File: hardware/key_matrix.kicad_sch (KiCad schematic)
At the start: 2 parts, among them SW3 Key

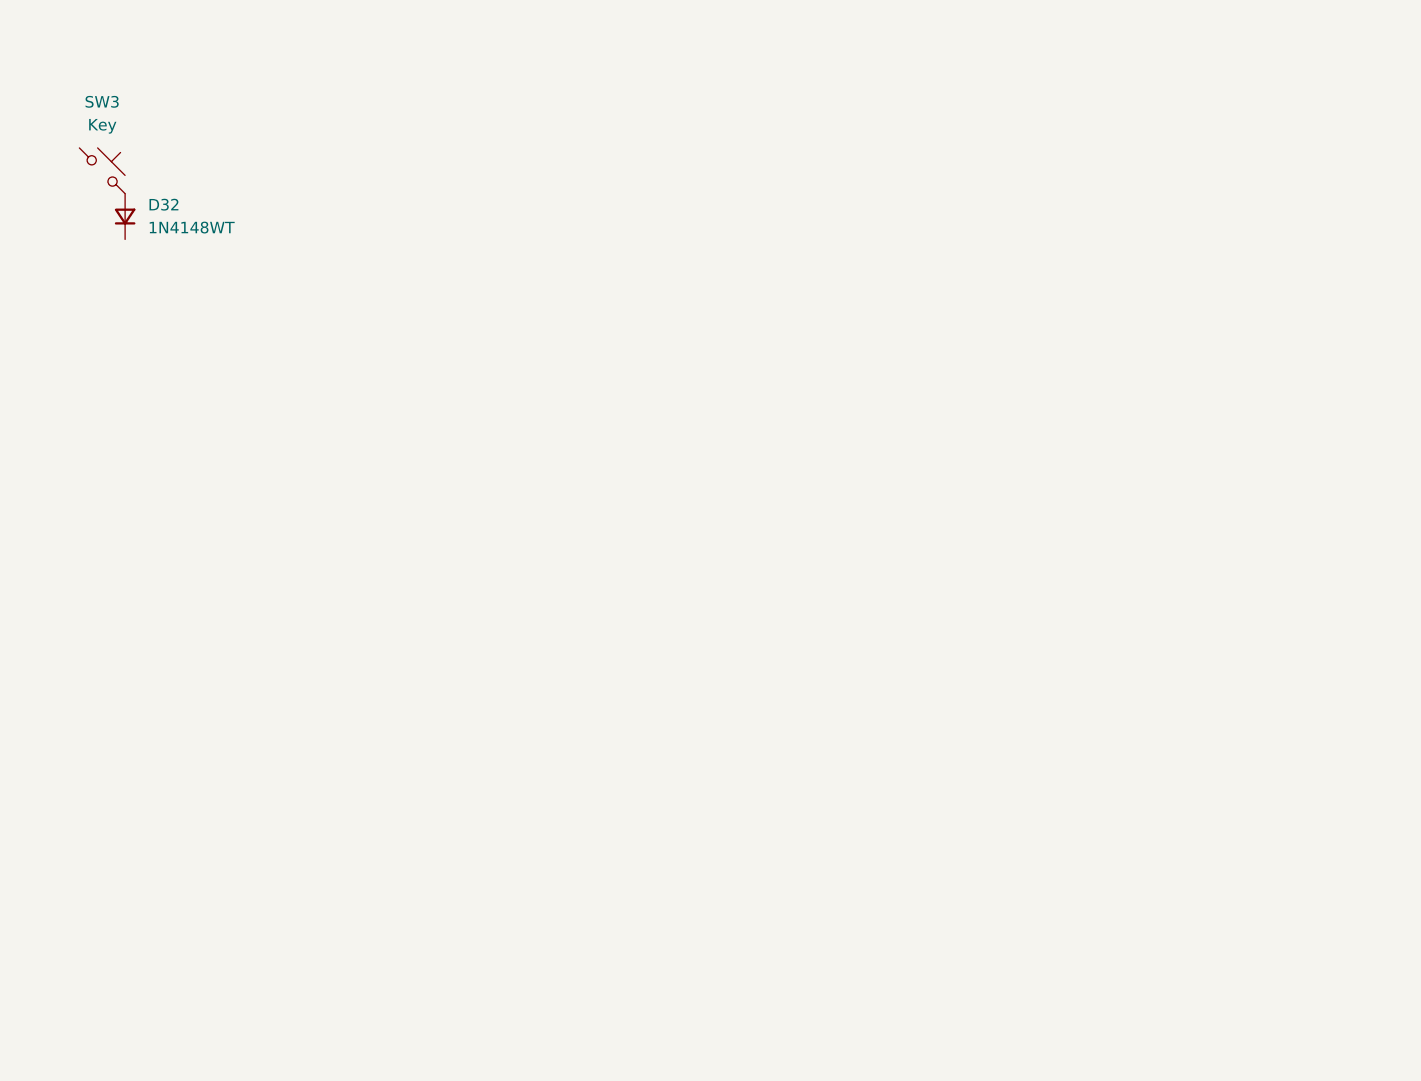
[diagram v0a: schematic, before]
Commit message: separate left/right part design, schematic
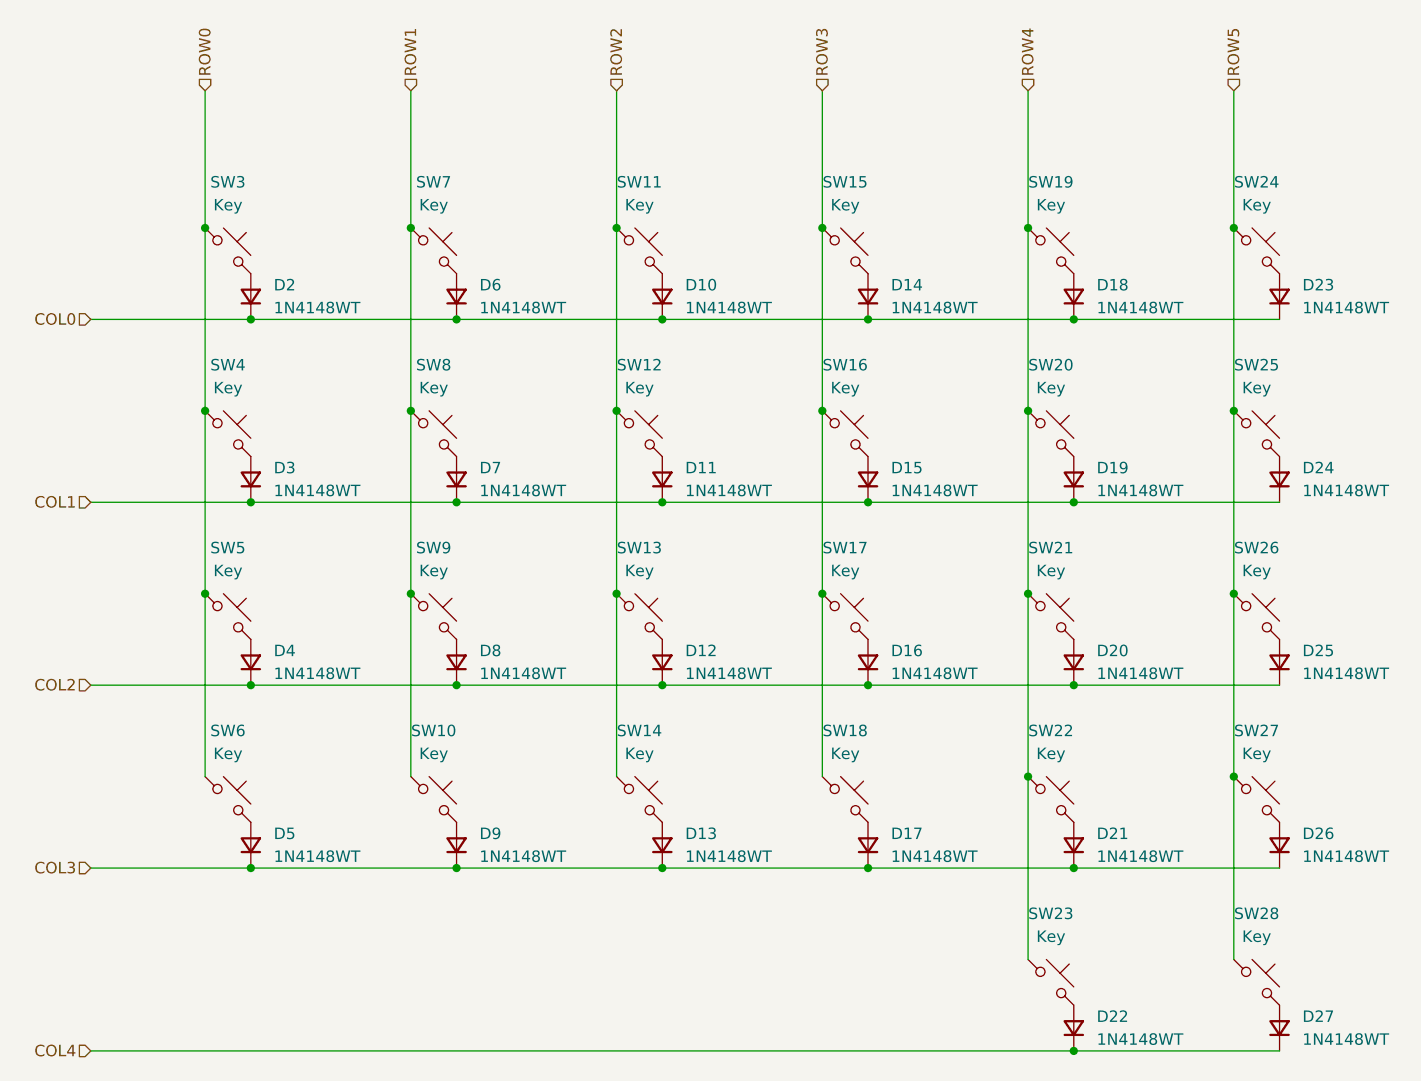
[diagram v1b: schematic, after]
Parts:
- added D10, D11, D12, D13, D14, D15, D16, D17, D18, D19, D20, D21, D22, D23, D24, D25, D26, D27, D3, D4, D5, D6, D7, D8, D9: 1N4148WT, PCM_Diode_SMD_AKL:D_SOD-523, symbol Device:D_Small
- added SW10, SW11, SW12, SW13, SW14, SW15, SW16, SW17, SW18, SW19, SW20, SW21, SW22, SW23, SW24, SW25, SW26, SW27, SW4, SW5, SW6, SW7, SW8, SW9: Key, rp_voyager:Gateron-KS33-Solderable-1U, symbol Switch:SW_Push_45deg
- added SW28: Key, rp_voyager:Gateron-KS33-Solderable-1x1.5U, symbol Switch:SW_Push_45deg
- SW3: footprint (none) -> rp_voyager:Gateron-KS33-Solderable-1U
- renumbered D32 to D2
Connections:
- net ROW0: now reaches SW3.1
- net ROW0: now also SW4.1, SW5.1, SW6.1
- net COL0: now reaches D2.1 (K)
- net COL0: now also D10.1 (K), D14.1 (K), D18.1 (K), D23.1 (K), D6.1 (K)
- new net: D3.2 (A), SW4.2
- new net: D13.2 (A), SW14.2
- new net: D18.2 (A), SW19.2
- new net: D6.2 (A), SW7.2
- new net: D10.2 (A), SW11.2
- new net: D14.2 (A), SW15.2
- new net: D22.2 (A), SW23.2
- new net: D19.2 (A), SW20.2
- new net: D23.2 (A), SW24.2
- new net: D16.2 (A), SW17.2
- new net: D20.2 (A), SW21.2
- new net: D4.2 (A), SW5.2
- new net: D24.2 (A), SW25.2
- new net: D26.2 (A), SW27.2
- new net: D21.2 (A), SW22.2
- new net: D7.2 (A), SW8.2
- new net: D11.2 (A), SW12.2
- new net: D15.2 (A), SW16.2
- new net: D8.2 (A), SW9.2
- new net: D25.2 (A), SW26.2
- new net: D5.2 (A), SW6.2
- new net: D12.2 (A), SW13.2
- new net: D17.2 (A), SW18.2
- new net: D9.2 (A), SW10.2
- new net: D27.2 (A), SW28.2
- new net COL1: D11.1 (K), D15.1 (K), D19.1 (K), D24.1 (K), D3.1 (K), D7.1 (K)
- new net COL2: D12.1 (K), D16.1 (K), D20.1 (K), D25.1 (K), D4.1 (K), D8.1 (K)
- new net COL3: D13.1 (K), D17.1 (K), D21.1 (K), D26.1 (K), D5.1 (K), D9.1 (K)
- new net COL4: D22.1 (K), D27.1 (K)
- new net ROW1: SW10.1, SW7.1, SW8.1, SW9.1
- new net ROW2: SW11.1, SW12.1, SW13.1, SW14.1
- new net ROW3: SW15.1, SW16.1, SW17.1, SW18.1
- new net ROW4: SW19.1, SW20.1, SW21.1, SW22.1, SW23.1
- new net ROW5: SW24.1, SW25.1, SW26.1, SW27.1, SW28.1
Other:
- moved on the sheet: D2, SW3

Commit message: encoder to schematic
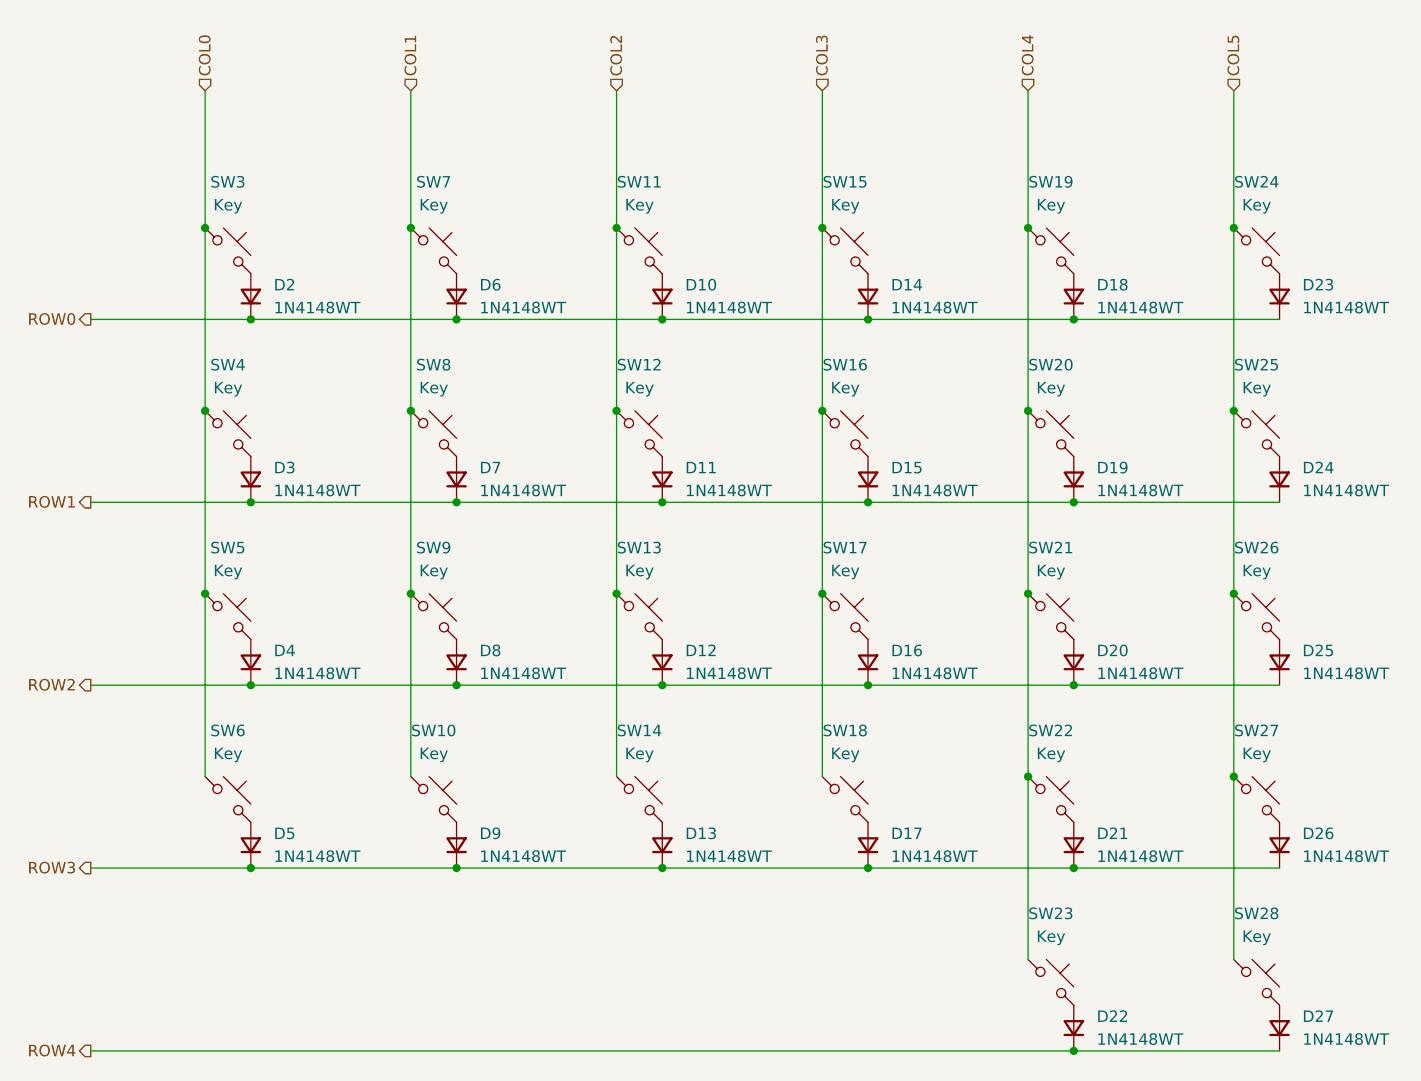
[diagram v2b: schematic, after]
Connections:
- net COL0: now also SW3.1, SW4.1, SW5.1, SW6.1; no longer D10.1 (K), D14.1 (K), D18.1 (K), D2.1 (K), D23.1 (K), D6.1 (K)
- net COL1: now also SW10.1, SW7.1, SW8.1, SW9.1; no longer D11.1 (K), D15.1 (K), D19.1 (K), D24.1 (K), D3.1 (K), D7.1 (K)
- net COL2: now also SW11.1, SW12.1, SW13.1, SW14.1; no longer D12.1 (K), D16.1 (K), D20.1 (K), D25.1 (K), D4.1 (K), D8.1 (K)
- net COL3: now also SW15.1, SW16.1, SW17.1, SW18.1; no longer D13.1 (K), D17.1 (K), D21.1 (K), D26.1 (K), D5.1 (K), D9.1 (K)
- net COL4: now also SW19.1, SW20.1, SW21.1, SW22.1, SW23.1; no longer D22.1 (K), D27.1 (K)
- net ROW0: now also D10.1 (K), D14.1 (K), D18.1 (K), D2.1 (K), D23.1 (K), D6.1 (K); no longer SW3.1, SW4.1, SW5.1, SW6.1
- net ROW1: now also D11.1 (K), D15.1 (K), D19.1 (K), D24.1 (K), D3.1 (K), D7.1 (K); no longer SW10.1, SW7.1, SW8.1, SW9.1
- net ROW2: now also D12.1 (K), D16.1 (K), D20.1 (K), D25.1 (K), D4.1 (K), D8.1 (K); no longer SW11.1, SW12.1, SW13.1, SW14.1
- net ROW3: now also D13.1 (K), D17.1 (K), D21.1 (K), D26.1 (K), D5.1 (K), D9.1 (K); no longer SW15.1, SW16.1, SW17.1, SW18.1
- net ROW4: now also D22.1 (K), D27.1 (K); no longer SW19.1, SW20.1, SW21.1, SW22.1, SW23.1
- net ROW5 renamed COL5
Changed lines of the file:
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@@
 		)
 	)
-	(hierarchical_label "ROW4"
+	(hierarchical_label "COL4"
 		(shape input)
 		(at 181.61 40.64 90)
@@
 		)
 	)
-	(hierarchical_label "COL1"
-		(shape input)
+	(hierarchical_label "ROW1"
+		(shape output)
 		(at 77.47 86.36 180)
 		(effects
@@
 		)
 	)
-	(hierarchical_label "ROW2"
+	(hierarchical_label "COL2"
 		(shape input)
 		(at 135.89 40.64 90)
@@
 		)
 	)
-	(hierarchical_label "ROW5"
+	(hierarchical_label "COL5"
 		(shape input)
 		(at 204.47 40.64 90)
@@
 		)
 	)
-	(hierarchical_label "ROW0"
+	(hierarchical_label "COL0"
 		(shape input)
 		(at 90.17 40.64 90)
@@
 		)
 	)
-	(hierarchical_label "COL0"
-		(shape input)
+	(hierarchical_label "ROW0"
+		(shape output)
 		(at 77.47 66.04 180)
 		(effects
@@
 		)
 	)
-	(hierarchical_label "COL2"
-		(shape input)
+	(hierarchical_label "ROW2"
+		(shape output)
 		(at 77.47 106.68 180)
 		(effects
@@
 		)
 	)
-	(hierarchical_label "ROW3"
+	(hierarchical_label "COL3"
 		(shape input)
 		(at 158.75 40.64 90)
@@
 		)
 	)
-	(hierarchical_label "ROW1"
+	(hierarchical_label "COL1"
 		(shape input)
 		(at 113.03 40.64 90)
@@
 		)
 	)
-	(hierarchical_label "COL3"
-		(shape input)
+	(hierarchical_label "ROW3"
+		(shape output)
 		(at 77.47 127 180)
 		(effects
@@
 		)
 	)
-	(hierarchical_label "COL4"
-		(shape input)
+	(hierarchical_label "ROW4"
+		(shape output)
 		(at 77.47 147.32 180)
 		(effects

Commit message: electronics
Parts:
- renumbered D7 to D10, D8 to D11, D9 to D12, D10 to D13, D11 to D14, D12 to D15, D13 to D16, D14 to D17, D15 to D18, D16 to D19, D17 to D20, D18 to D21, D19 to D22, D20 to D23, D21 to D24, D22 to D25, D23 to D26, D24 to D27, D25 to D28, D26 to D29, D27 to D30, D2 to D5, D3 to D6, D4 to D7, D5 to D8, D6 to D9
